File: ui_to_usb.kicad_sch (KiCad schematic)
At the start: 39 parts, among them J1 TYPE-C-31-M-12, J2 PM254-2-06-S-8.5, J3 BM12B-SRSS-TB, SW1 TS24CA, SW2 TS24CA, U1 SPX3819M5-L, U2 USBLC6-2SC6, U3 CH32V203K8T6, Y1 8M

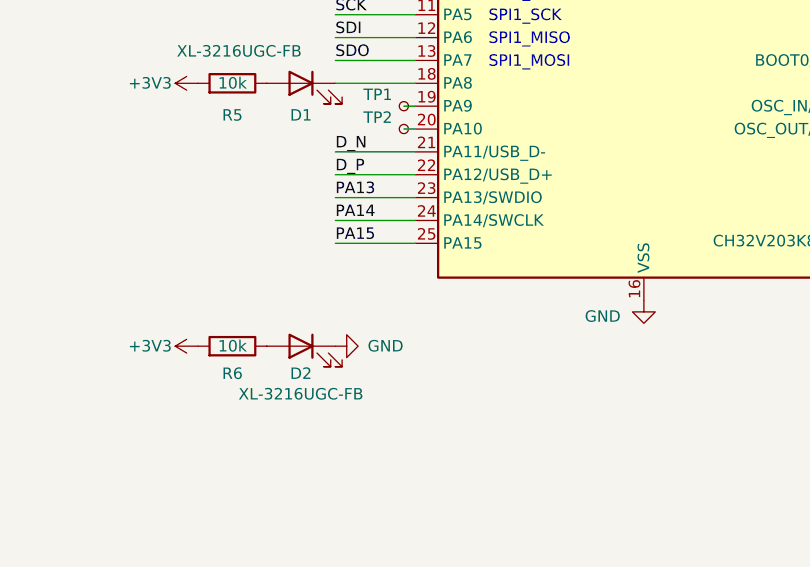
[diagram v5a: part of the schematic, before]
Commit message: moved tactile buttons because of colission with shroud on ui_board_1u
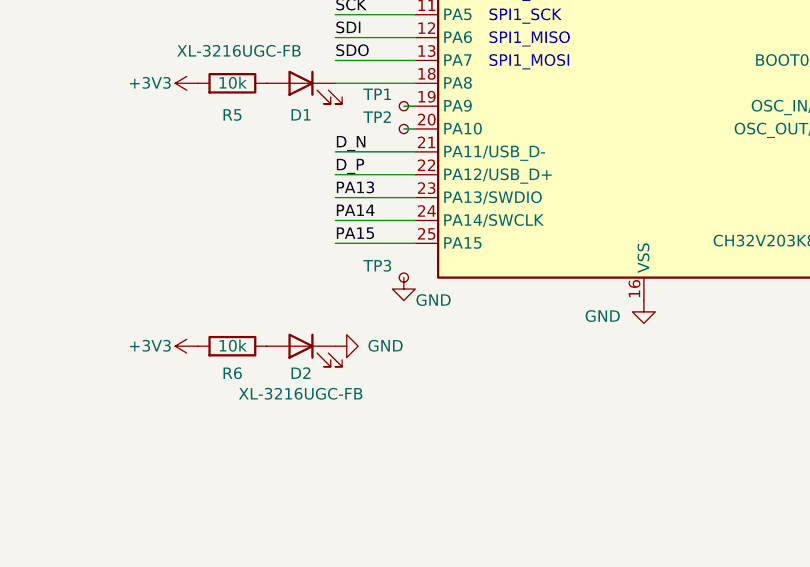
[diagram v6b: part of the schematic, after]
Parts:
- added TP3: GND, TestPoint:TestPoint_Pad_D1.0mm, symbol Connector:TestPoint_Small
- TP1: value U_TX -> A9
- TP2: value U_RX -> A10
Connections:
- net GND: now also TP3.1
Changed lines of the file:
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@@
 			)
 		)
-		(property "Value" "U_TX"
+		(property "Value" "A9"
 			(at 119.888 125.476 0)
 			(effects
@@
 	)
 	(symbol
+		(lib_id "power:GND")
+		(at 114.3 142.24 0)
+		(mirror y)
+		(unit 1)
+		(exclude_from_sim no)
+		(in_bom yes)
+		(on_board yes)
+		(dnp no)
+		(property "Reference" "#PWR043"
+			(at 114.3 148.59 0)
+			(effects
+				(font
+					(size 1.27 1.27)
+				)
+				(hide yes)
+			)
+		)
+		(property "Value" "GND"
+			(at 117.602 144.78 0)
+			(effects
+				(font
+					(size 1.27 1.27)
+				)
+			)
+		)
+		(property "Footprint" ""
+			(at 114.3 142.24 0)
+			(effects
+				(font
+					(size 1.27 1.27)
+				)
+				(hide yes)
+			)
+		)
+		(property "Datasheet" ""
+			(at 114.3 142.24 0)
+			(effects
+				(font
+					(size 1.27 1.27)
+				)
+				(hide yes)
+			)
+		)
+		(property "Description" "Power symbol creates a global label with name \"GND\" , ground"
+			(at 114.3 142.24 0)
+			(effects
+				(font
+					(size 1.27 1.27)
+				)
+				(hide yes)
+			)
+		)
+		(pin "1"
+		)
+		(instances
+			(project "ui_to_usb"
+				(path "/61164785-2abe-4800-8948-e7ba22968736"
+					(reference "#PWR043")
+					(unit 1)
+				)
+			)
+		)
+	)
+	(symbol
 		(lib_id "power:PWR_FLAG")
 		(at 67.31 35.56 270)
@@
 	)
 	(symbol
+		(lib_id "Connector:TestPoint_Small")
+		(at 114.3 142.24 0)
+		(unit 1)
+		(exclude_from_sim no)
+		(in_bom yes)
+		(on_board yes)
+		(dnp no)
+		(property "Reference" "TP3"
+			(at 113.03 140.9699 0)
+			(effects
+				(font
+					(size 1.27 1.27)
+				)
+				(justify right)
+			)
+		)
+		(property "Value" "GND"
+			(at 119.888 144.526 0)
+			(effects
+				(font
+					(size 1.27 1.27)
+				)
+				(justify right)
+				(hide yes)
+			)
+		)
+		(property "Footprint" "TestPoint:TestPoint_Pad_D1.0mm"
+			(at 119.38 142.24 0)
+			(effects
+				(font
+					(size 1.27 1.27)
+				)
+				(hide yes)
+			)
+		)
+		(property "Datasheet" "~"
+			(at 119.38 142.24 0)
+			(effects
+				(font
+					(size 1.27 1.27)
+				)
+				(hide yes)
+			)
+		)
+		(property "Description" "test point"
+			(at 114.3 142.24 0)
+			(effects
+				(font
+					(size 1.27 1.27)
+				)
+				(hide yes)
+			)
+		)
+		(pin "1"
+		)
+		(instances
+			(project "ui_to_usb"
+				(path "/61164785-2abe-4800-8948-e7ba22968736"
+					(reference "TP3")
+					(unit 1)
+				)
+			)
+		)
+	)
+	(symbol
 		(lib_id "power:+3V3")
 		(at 142.24 72.39 0)
@@
 			)
 		)
-		(property "Value" "U_RX"
+		(property "Value" "A10"
 			(at 119.888 128.016 0)
 			(effects

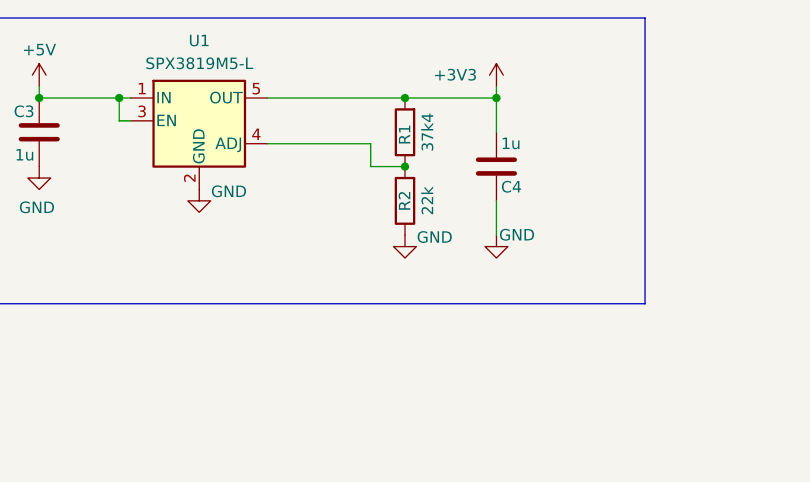
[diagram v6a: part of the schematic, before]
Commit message: change 3V3 feedback resistor for more common values
sent for production
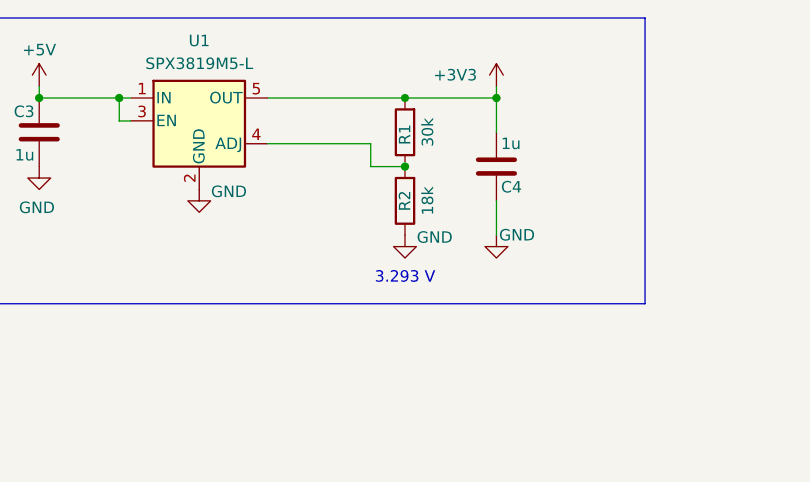
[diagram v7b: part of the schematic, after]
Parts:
- R1: value 37k4 -> 30k
- R2: value 22k -> 18k
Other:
- note added: "3.293 V"
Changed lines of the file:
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@@
 		)
 	)
+	(text "3.293 V"
+		(exclude_from_sim no)
+		(at 224.79 54.356 0)
+		(effects
+			(font
+				(size 1.27 1.27)
+			)
+		)
+	)
 	(text "Extension Port"
 		(exclude_from_sim no)
@@
 			)
 		)
-		(property "Value" "22k"
+		(property "Value" "18k"
 			(at 227.33 45.72 90)
 			(effects
@@
 			)
 		)
-		(property "Value" "37k4"
+		(property "Value" "30k"
 			(at 227.33 38.1 90)
 			(effects
